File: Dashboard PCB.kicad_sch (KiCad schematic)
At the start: 47 parts, among them J1 Controls_Leader_Export_02x06, J5 Horn_In_01x02, J6 Horn_Out_01x02, J8 Supp_Out, J9 Supp_In, Q1 TO200P800X182-5N, Q2 Q_PMOS_GDS

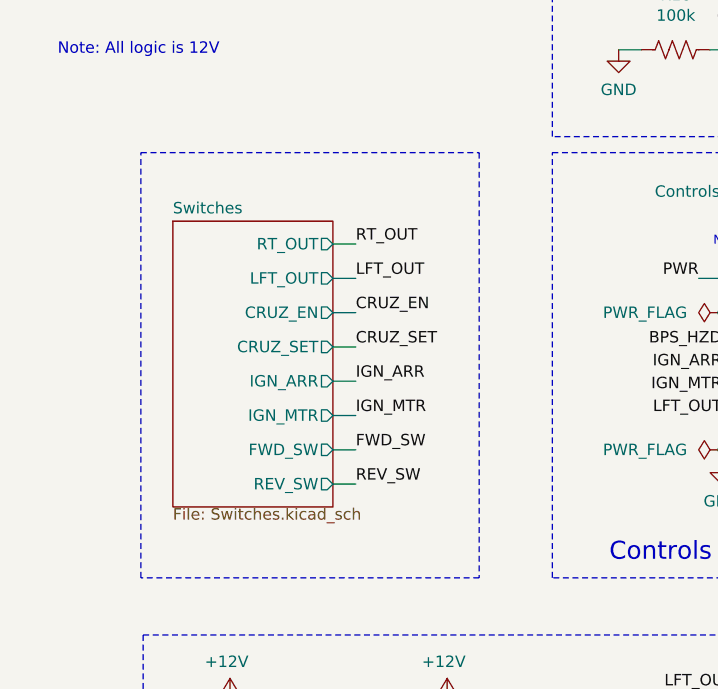
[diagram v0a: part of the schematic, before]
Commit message: make ign off cruz en or some shit
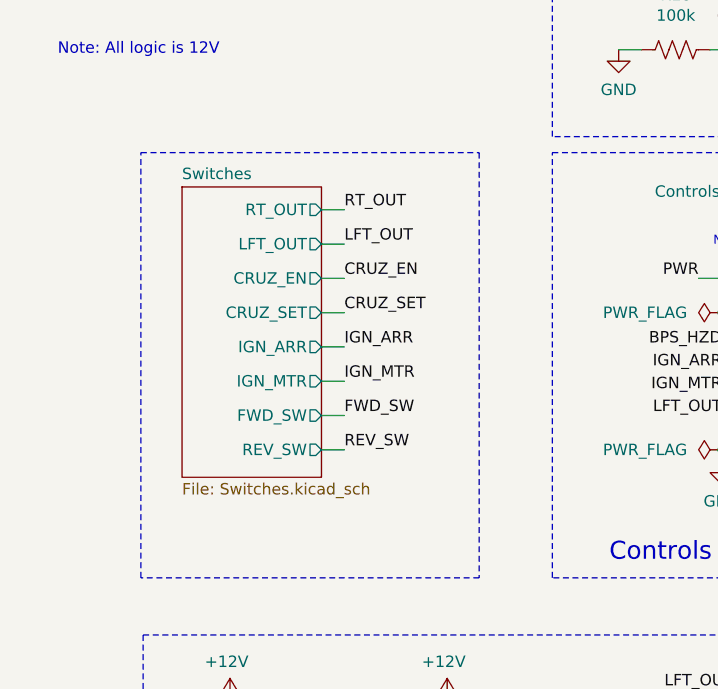
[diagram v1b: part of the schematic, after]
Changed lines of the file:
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@@
 	(wire
 		(pts
-			(xy 54.61 93.98) (xy 52.07 93.98)
+			(xy 53.34 90.17) (xy 50.8 90.17)
 		)
 		(stroke
@@
 	(wire
 		(pts
-			(xy 52.07 71.12) (xy 54.61 71.12)
+			(xy 50.8 67.31) (xy 53.34 67.31)
 		)
 		(stroke
@@
 	(wire
 		(pts
-			(xy 54.61 90.17) (xy 52.07 90.17)
+			(xy 53.34 86.36) (xy 50.8 86.36)
 		)
 		(stroke
@@
 	(wire
 		(pts
-			(xy 54.61 78.74) (xy 52.07 78.74)
+			(xy 53.34 74.93) (xy 50.8 74.93)
 		)
 		(stroke
@@
 	(wire
 		(pts
-			(xy 54.61 97.79) (xy 52.07 97.79)
+			(xy 53.34 93.98) (xy 50.8 93.98)
 		)
 		(stroke
@@
 	(wire
 		(pts
-			(xy 54.61 86.36) (xy 52.07 86.36)
+			(xy 53.34 82.55) (xy 50.8 82.55)
 		)
 		(stroke
@@
 	(wire
 		(pts
-			(xy 54.61 82.55) (xy 52.07 82.55)
+			(xy 53.34 78.74) (xy 50.8 78.74)
 		)
 		(stroke
@@
 	(wire
 		(pts
-			(xy 54.61 74.93) (xy 52.07 74.93)
+			(xy 53.34 71.12) (xy 50.8 71.12)
 		)
 		(stroke
@@
 	)
 	(label "CRUZ_SET"
-		(at 54.61 82.55 0)
+		(at 53.34 78.74 0)
 		(fields_autoplaced yes)
 		(effects
@@
 	)
 	(label "REV_SW"
-		(at 54.61 97.79 0)
+		(at 53.34 93.98 0)
 		(fields_autoplaced yes)
 		(effects
@@
 	)
 	(label "CRUZ_EN"
-		(at 54.61 78.74 0)
+		(at 53.34 74.93 0)
 		(fields_autoplaced yes)
 		(effects
@@
 	)
 	(label "FWD_SW"
-		(at 54.61 93.98 0)
+		(at 53.34 90.17 0)
 		(fields_autoplaced yes)
 		(effects
@@
 	)
 	(label "IGN_MTR"
-		(at 54.61 90.17 0)
+		(at 53.34 86.36 0)
 		(fields_autoplaced yes)
 		(effects
@@
 	)
 	(label "LFT_OUT"
-		(at 54.61 74.93 0)
+		(at 53.34 71.12 0)
 		(fields_autoplaced yes)
 		(effects
@@
 	)
 	(label "IGN_ARR"
-		(at 54.61 86.36 0)
+		(at 53.34 82.55 0)
 		(fields_autoplaced yes)
 		(effects
@@
 	)
 	(label "RT_OUT"
-		(at 54.61 71.12 0)
+		(at 53.34 67.31 0)
 		(fields_autoplaced yes)
 		(effects
@@
 	)
 	(sheet
-		(at 34.29 68.58)
-		(size 17.78 31.75)
+		(at 35.306 64.77)
+		(size 15.494 32.258)
 		(fields_autoplaced yes)
 		(stroke
@@
 		)
 		(property "Sheetname" "Switches"
-			(at 34.29 67.8684 0)
+			(at 35.306 64.0584 0)
 			(effects
 				(font
@@
 		)
 		(property "Sheetfile" "Switches.kicad_sch"
-			(at 34.29 100.4066 0)
+			(at 35.306 97.6126 0)
 			(effects
 				(font
@@
 		)
 		(pin "RT_OUT" output
-			(at 52.07 71.12 0)
+			(at 50.8 67.31 0)
 			(effects
 				(font
@@
 		)
 		(pin "LFT_OUT" output
-			(at 52.07 74.93 0)
+			(at 50.8 71.12 0)
 			(effects
 				(font
@@
 		)
 		(pin "CRUZ_EN" output
-			(at 52.07 78.74 0)
+			(at 50.8 74.93 0)
 			(effects
 				(font
@@
 		)
 		(pin "CRUZ_SET" output
-			(at 52.07 82.55 0)
+			(at 50.8 78.74 0)
 			(effects
 				(font
@@
 		)
 		(pin "IGN_ARR" output
-			(at 52.07 86.36 0)
+			(at 50.8 82.55 0)
 			(effects
 				(font
@@
 		)
 		(pin "IGN_MTR" output
-			(at 52.07 90.17 0)
+			(at 50.8 86.36 0)
 			(effects
 				(font
@@
 		)
 		(pin "FWD_SW" output
-			(at 52.07 93.98 0)
+			(at 50.8 90.17 0)
 			(effects
 				(font
@@
 		)
 		(pin "REV_SW" output
-			(at 52.07 97.79 0)
+			(at 50.8 93.98 0)
 			(effects
 				(font
